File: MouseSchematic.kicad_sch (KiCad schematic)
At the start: 21 parts, among them IC1 AZ1117IH-3.3TRG1, J1 JST1, J2 JST2, J3 Left Header, J4 Right Header, Q1 MOSFET, Q2 IR Receiver, U1 L293DD

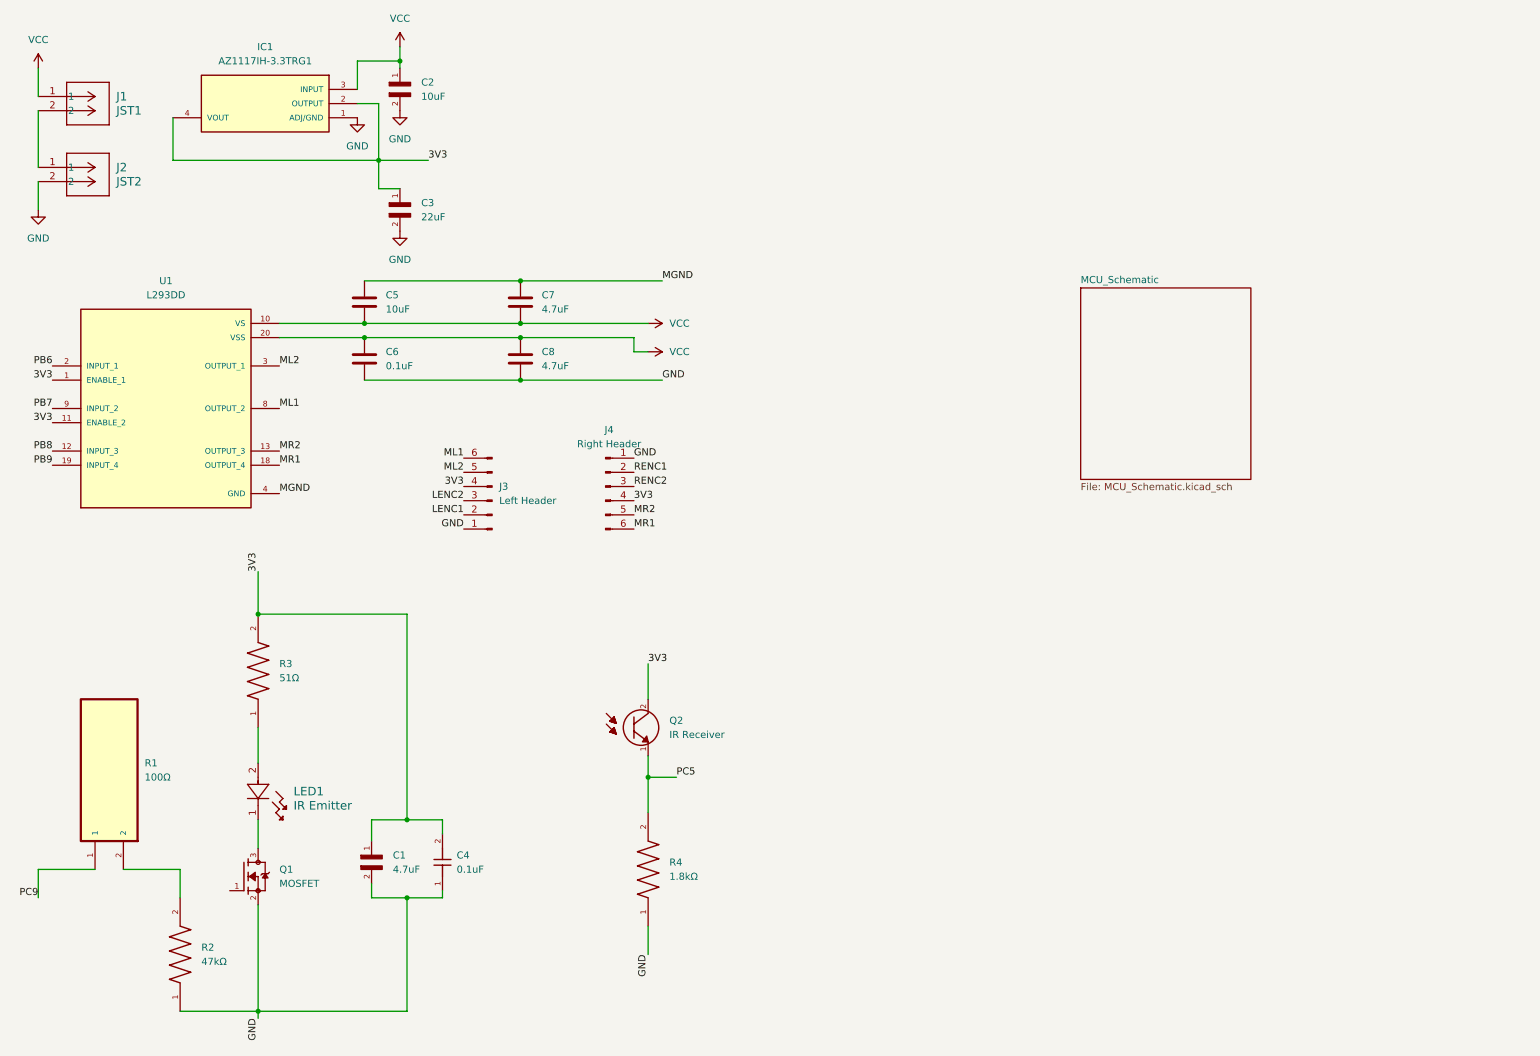
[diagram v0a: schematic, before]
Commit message: Added microcontroller, organized
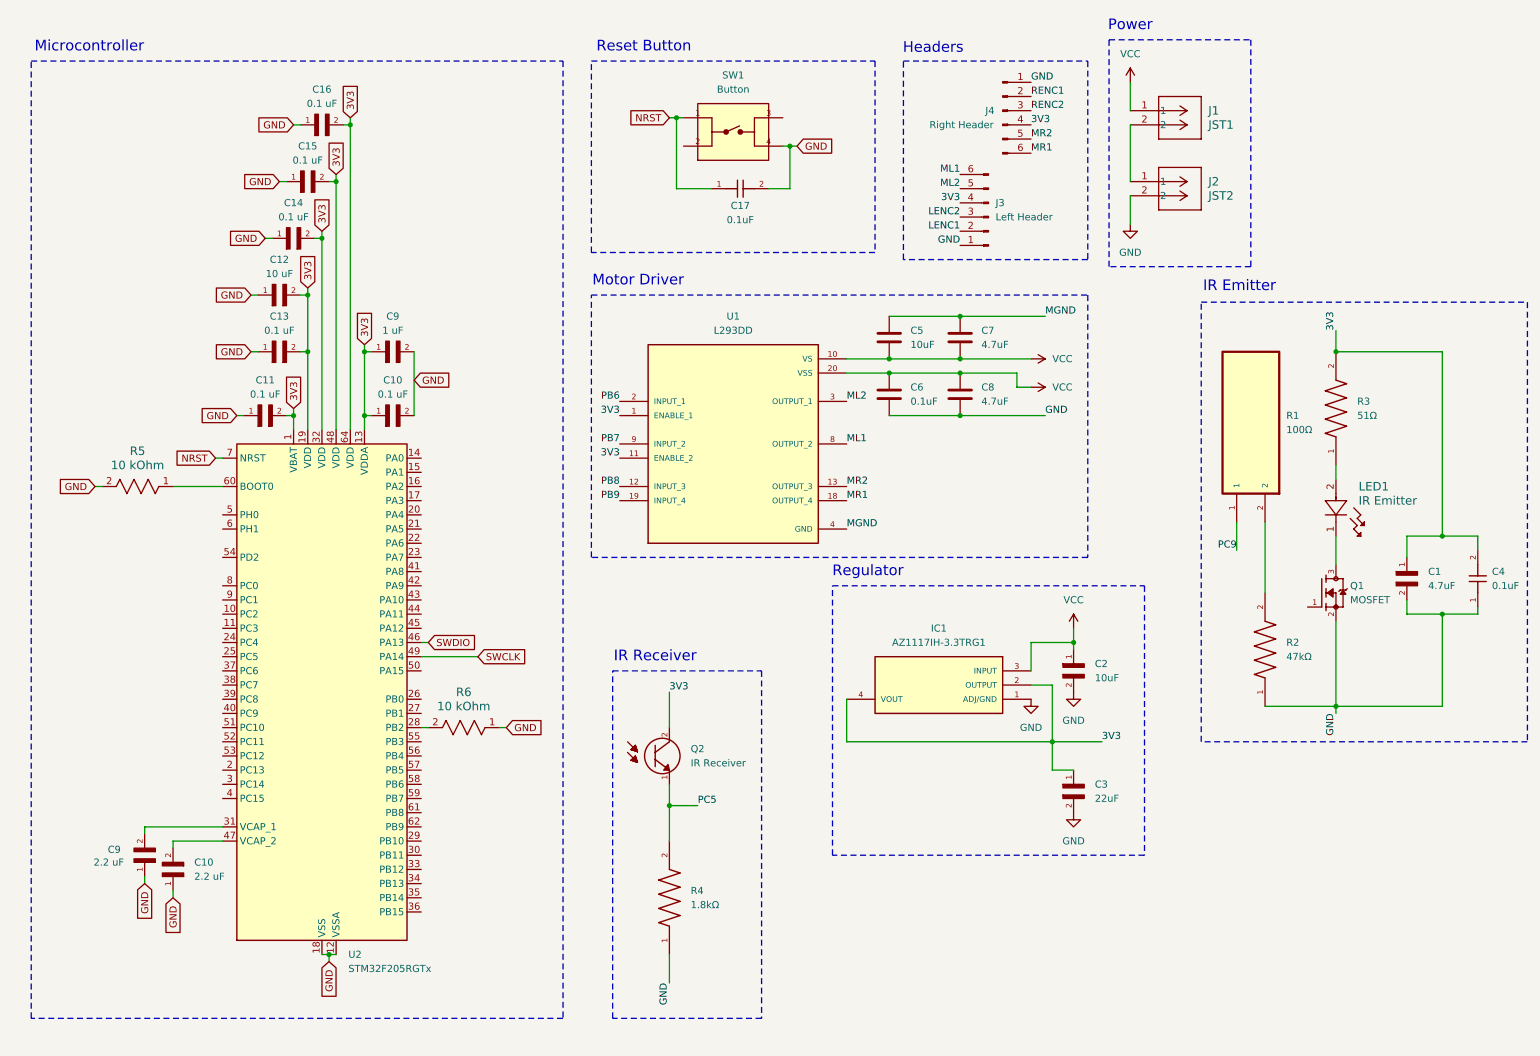
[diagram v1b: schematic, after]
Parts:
- added C10, C9: 2.2 uF, 10uF_Capacitor_FP_GRM188R61C106MAALD:CAPC1608X95N, symbol 10uF_Capacitor_GRM188R61C106MAALD:GRM188R61C106MAALD
- added C10, C11, C13, C14, C15, C16: 0.1 uF, 10uF_Capacitor_FP_GRM188R61C106MAALD:CAPC1608X95N, symbol 10uF_Capacitor_GRM188R61C106MAALD:GRM188R61C106MAALD
- added C12: 10 uF, 10uF_Capacitor_FP_GRM188R61C106MAALD:CAPC1608X95N, symbol 10uF_Capacitor_GRM188R61C106MAALD:GRM188R61C106MAALD
- added C17: 0.1uF, C0805C104K5RACTU:CAPC2012X88N, symbol Capacitor0.1u_C0805C104K5RACTU:C0805C104K5RACTU
- added C9: 1 uF, 10uF_Capacitor_FP_GRM188R61C106MAALD:CAPC1608X95N, symbol 10uF_Capacitor_GRM188R61C106MAALD:GRM188R61C106MAALD
- added R5, R6: 10 kOhm, 51Ohm_Resistor_FP:RES_RK73B_1J_KOA, symbol 51Ohm_Resistor:RK73B1JTTD510J
- added SW1: Button, Button_FP_FSM4JSMA:TE_FSM4JSMA, symbol Button_FSM4JSMA:FSM4JSMA
- added U2: STM32F205RGTx, Package_QFP:LQFP-64_10x10mm_P0.5mm, symbol MCU_ST_STM32F2:STM32F205RGTx
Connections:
- net 3V3: now also C10.1, C11.2, C12.2, C13.2, C14.2, C15.2, C16.2, C9.1, U2.1 (VBAT), U2.13 (VDDA), U2.19 (VDD), U2.32 (VDD), U2.48 (VDD), U2.64 (VDD)
- net GND: now also C10.1, C10.2, C11.1, C12.1, C13.1, C14.1, C15.1, C16.1, C17.2, C9.1, C9.2, R5.2, R6.1, SW1.4, U2.12 (VSSA), U2.18 (VSS), U2.63 (VSS)
- new net: C10.2, U2.47 (VCAP_2)
- new net: R6.2, U2.28 (PB2)
- new net: C9.2, U2.31 (VCAP_1)
- new net: R5.1, U2.60 (BOOT0)
- new net NRST: C17.1, SW1.1, U2.7 (NRST)
- new net SWCLK: U2.49 (PA14)
- new net SWDIO: U2.46 (PA13)
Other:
- removed sheet MCU_Schematic
- note added: "Headers"
- note added: "IR Emitter"
- note added: "IR Receiver"
- note added: "Microcontroller"
- note added: "Motor Driver"
- note added: "Power"
- note added: "Regulator"
- note added: "Reset Button"
- moved on the sheet: C1, C2, C3, C4, C5, C6, C7, C8, IC1, J1, J2, J3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

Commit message: Finished schematic wiring
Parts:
- added C18, C20, C22: 4.7uF, C2012X7R1C475K125AE:CAPC2012X150N, symbol Capacitor4.7u_C2012X7R1C475K125AE:C2012X7R1C475K125AE
- added C19, C21, C23: 0.1uF, C0805C104K5RACTU:CAPC2012X88N, symbol Capacitor0.1u_C0805C104K5RACTU:C0805C104K5RACTU
- added J6: Conn_01x04, symbol Connector_Generic:Conn_01x04
- added LED2, LED3, LED4: IR Emitter, LED_INL-5AMIR15_INO, symbol LED_IR_Emitter_INL-5AMIR15:INL-5AMIR15
- added Q3, Q4, Q5: IR Receiver, SFH_313_FA-3_4:XDCR_SFH_313_FA-3_4, symbol Phototransistor_SFH_313_FA-3_4:SFH_313_FA-3_4
- added Q6, Q7, Q8: MOSFET, 2N7002LT1G:SOT95P240X111-3N, symbol MOSFET_2N7002LT1G:2N7002LT1G
- added R10, R13, R16: 100Ω, ERA-6AEB101V:RESC2012X60N, symbol Resistor100_ERA-6AEB101V:ERA-6AEB101V
- added R11, R14, R17: 47kΩ, ERA6AEB473V:RES_ERA6AEB473V, symbol Resistor47k_ERA_6AEB473V:ERA6AEB473V
- added R12, R15, R18: 51Ω, RC0805FR-0751RL:RESC2012X60N, symbol Resistor51_RC0805FR-0751RL:RC0805FR-0751RL
- added R7, R8, R9: 1.8kΩ, RMCF0805JT1K80:RESC2012X65N, symbol Resistor1.8k_RMCF0805JT1K80:RMCF0805JT1K80
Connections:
- net PB6 is gone; now on an unnamed net: U1.2 (INPUT_1)
- net PB7 is gone; now on an unnamed net: U1.9 (INPUT_2)
- net PB8 is gone; now on an unnamed net: U1.12 (INPUT_3)
- net PB9 is gone; now on an unnamed net: U1.19 (INPUT_4)
- net PC9 is gone; now on an unnamed net: R1.1
- net 3V3: now also C18.1, C19.2, C20.1, C21.2, C22.1, C23.2, Q3.2, Q4.2, Q5.2, R12.2, R15.2, R18.2
- net GND: now also C18.2, C19.1, C20.2, C21.1, C22.2, C23.1, J6.3 (Pin_3), Q6.2, Q7.2, Q8.2, R11.1, R14.1, R17.1, R7.1, R8.1, R9.1
- net LENC1: now also U2.42 (PA9)
- net LENC2: now also U2.41 (PA8)
- net PC5: now also U2.25 (PC5)
- net RENC1: now also U2.15 (PA1)
- net RENC2: now also U2.14 (PA0)
- net SWCLK: now also J6.4 (Pin_4)
- net SWDIO: now also J6.2 (Pin_2)
- net NSRT: now reaches SW1.3
- net NSRT: now also J6.1 (Pin_1)
- net PA6: now reaches U2.22 (PA6)
- net PA6: now also Q4.1, R8.2
- net PA7: now reaches U2.23 (PA7)
- net PA7: now also R13.1
- net PC4: now reaches U2.24 (PC4)
- net PC4: now also Q3.1, R7.2
- net PB1: now reaches U2.27 (PB1)
- net PB1: now also Q5.1, R9.2
- net PB13: now reaches U2.34 (PB13)
- net PB13: now also R10.1
- net PB3: now reaches U2.55 (PB3)
- net PB3: now also R16.1
- new net: LED2.1, Q6.3
- new net: LED2.2, R12.1
- new net: R16.2, R17.2
- new net: LED3.1, Q7.3
- new net: LED3.2, R15.1
- new net: R13.2, R14.2
- new net: R10.2, R11.2
- new net: LED4.1, Q8.3
- new net: LED4.2, R18.1
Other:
- note added: "Front Left IR Emitter"
- note added: "Front Left IR Receiver"
- note added: "Left IR Emitter"
- note added: "Left IR Receiver"
- note added: "Right IR Emitter"
- note added: "Right IR Receiver"
- moved on the sheet: C1, C17, C2, C3, C4, C5, C6, C7, C8, IC1, J3, J4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

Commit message: Schematic review
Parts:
- removed C10, C11, C13, C14, C15, C16: 0.1 uF, 10uF_Capacitor_FP_GRM188R61C106MAALD:CAPC1608X95N, symbol 10uF_Capacitor_GRM188R61C106MAALD:GRM188R61C106MAALD
- added C10, C12, C4, C5, C6, C7: 0.1uF, C0805C104K5RACTU:CAPC2012X88N, symbol Capacitor0.1u_C0805C104K5RACTU:C0805C104K5RACTU
- J4: renamed from J1; footprint CONN2_B2B-PH-K-S_JST -> B2B-PH-K-S:CONN2_B2B-PH-K-S_JST
- J5: renamed from J2; footprint CONN2_B2B-PH-K-S_JST -> B2B-PH-K-S:CONN2_B2B-PH-K-S_JST
- LED1, LED2, LED3, LED4: footprint LED_INL-5AMIR15_INO -> INL-5AMIR15:LED_INL-5AMIR15_INO
- renumbered C17 to C1, C4 to C11, C9 to C13, C8 to C14, C7 to C15, C6 to C16, C5 to C17, C19 to C18, C18 to C19, C9 to C2, C2 to C24, C3 to C25, C10 to C3, C12 to C8, C1 to C9, J6 to J1, J3 to J2, J4 to J3, Q6 to Q4, Q4 to Q5, Q7 to Q6, Q8 to Q7, Q5 to Q8, R13 to R11, R14 to R12, R8 to R13, R15 to R14, R16 to R15, R17 to R16, R18 to R17, R9 to R18, R5 to R3, R3 to R4, R6 to R5, R4 to R6, R12 to R8, R11 to R9, U2 to U1, U1 to U2
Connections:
- net 3V3: now also C10.2, C12.1, C4.2, C5.2, C6.2, C7.2
- net GND: now also C10.1, C12.2, C4.1, C5.1, C6.1, C7.1
- net at R15.2, R16.2: now also Q7.1
- net at R1.2, R2.2: now also Q1.1
- net at R11.2, R12.2: now also Q6.1
- net at R10.2, R9.2: now also Q4.1
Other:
- moved on the sheet: C1, C11, C13, C14, C15, C16, C17, C18, C19, C2, C20, C21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

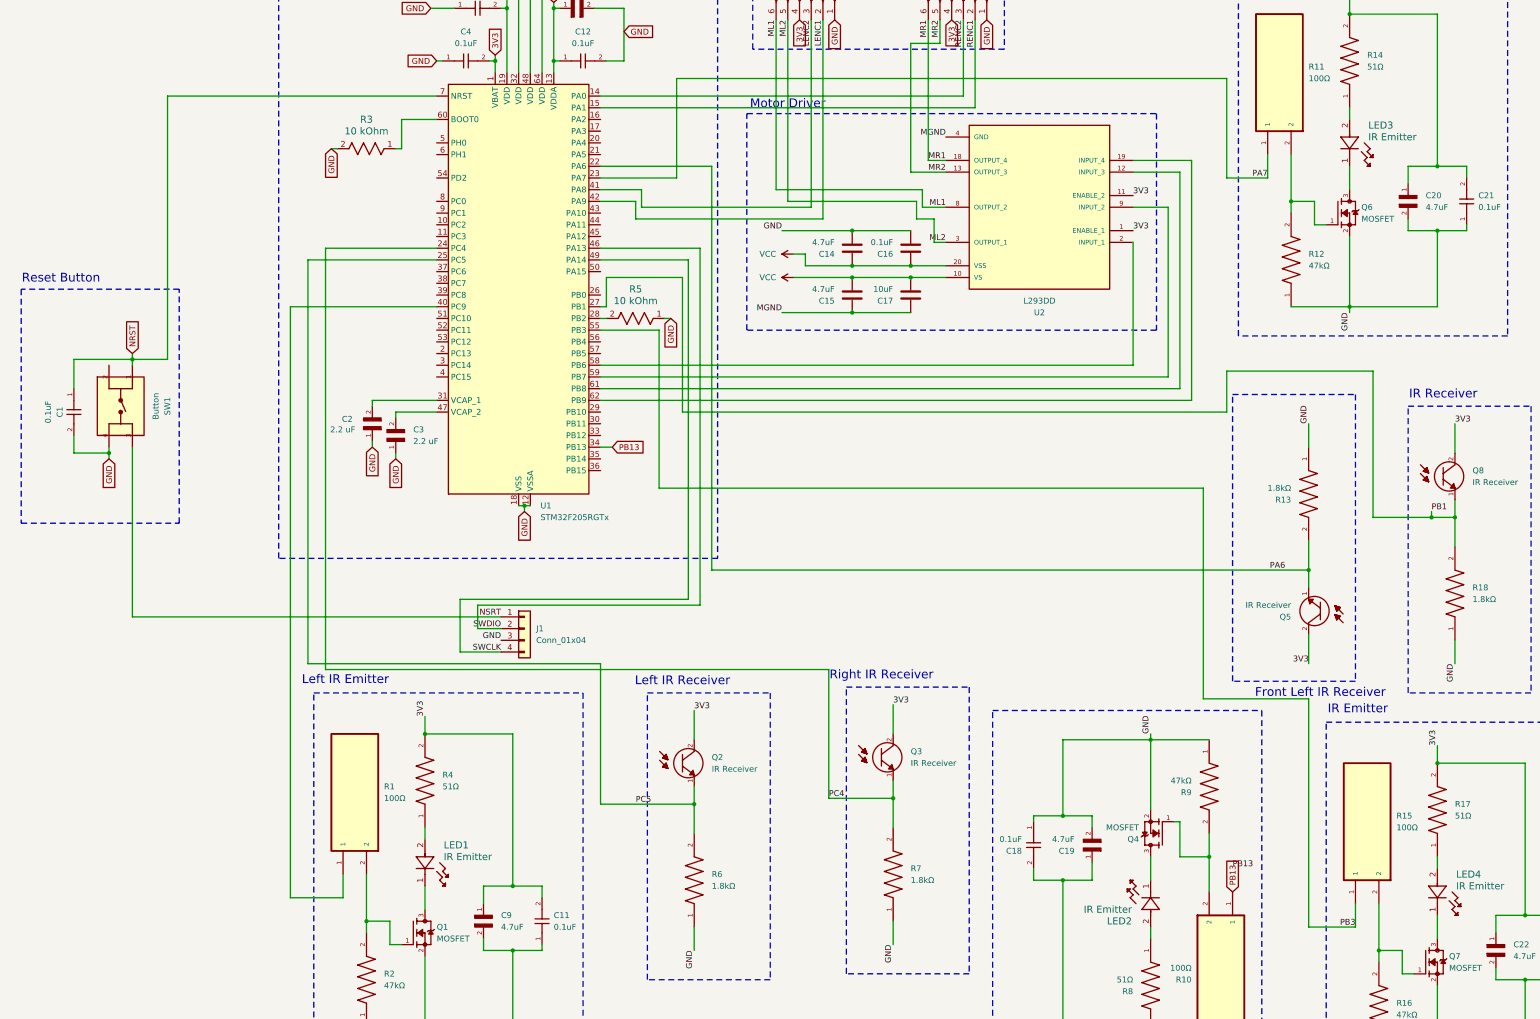
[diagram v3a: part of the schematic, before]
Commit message: Update schematic with more global labels (still need to finish reviewing)
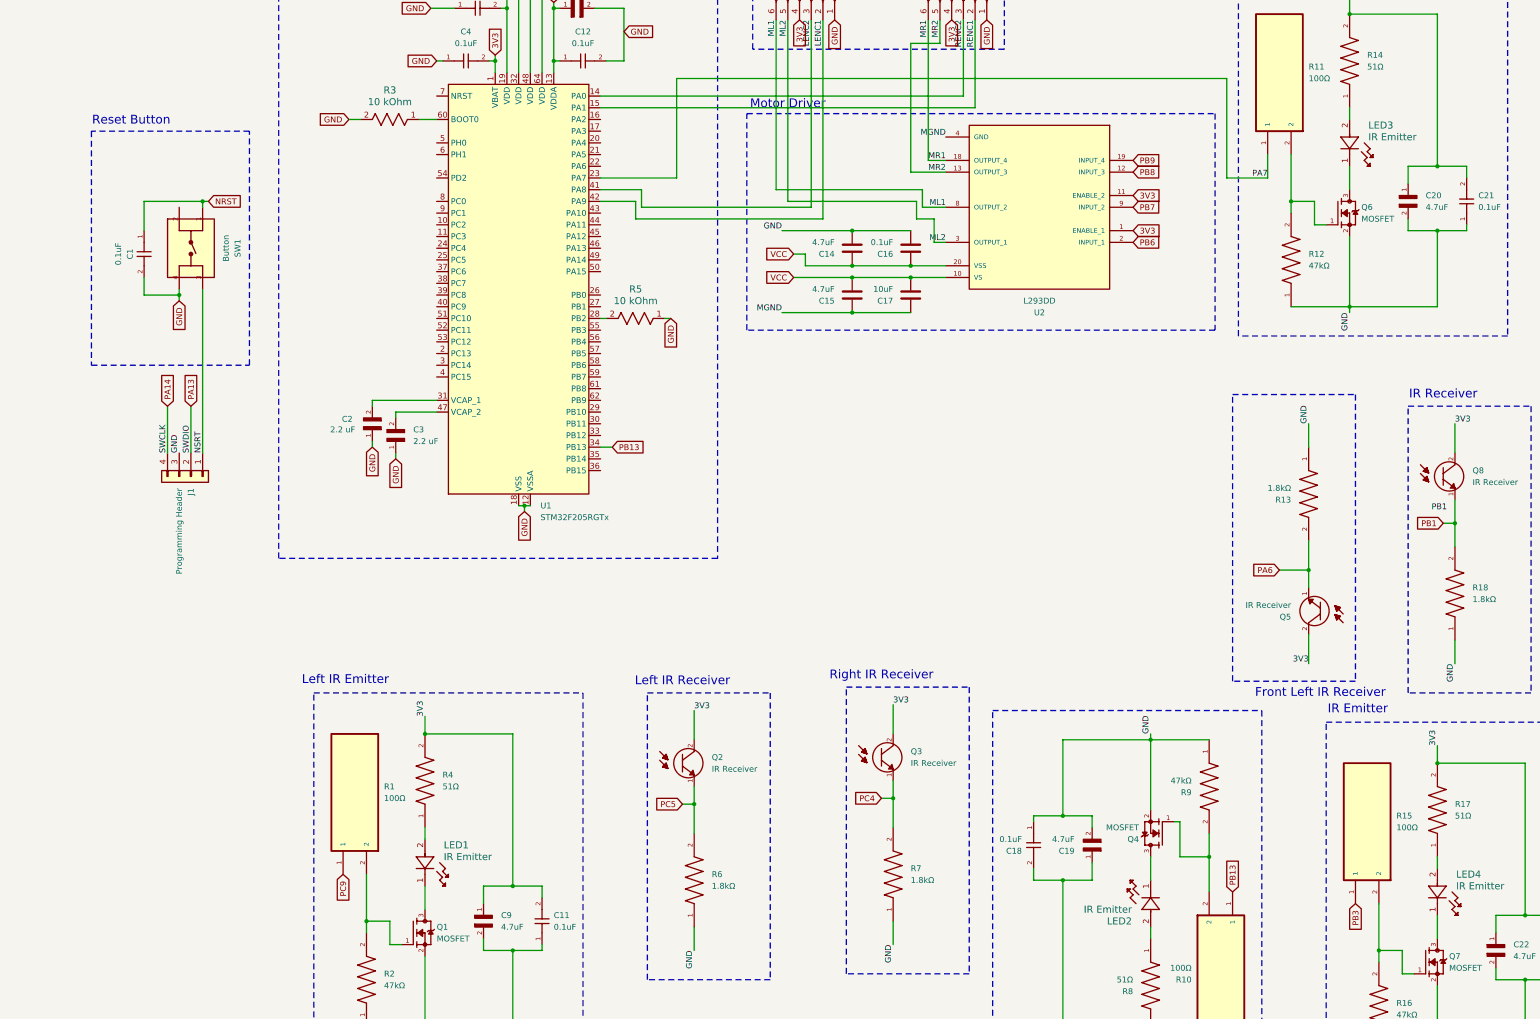
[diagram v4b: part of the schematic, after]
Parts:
- J1: value Conn_01x04 -> Programming Header
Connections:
- net NRST: no longer U1.7 (NRST)
- net PA6: no longer U1.22 (PA6)
- net PB1: no longer U1.27 (PB1)
- net PB3: no longer U1.55 (PB3)
- net PC4: no longer U1.24 (PC4)
- net PC5: no longer U1.25 (PC5)
- net at U1.40 (PC9): no longer R1.1
- net at U1.58 (PB6): no longer U2.2 (INPUT_1)
- net at U1.59 (PB7): no longer U2.9 (INPUT_2)
- net at U1.61 (PB8): no longer U2.12 (INPUT_3)
- net at U1.62 (PB9): no longer U2.19 (INPUT_4)
- net SWCLK: no longer names the net of U1.49 (PA14)
- net SWCLK: no longer J1.4 (Pin_4)
- net SWDIO: no longer names the net of U1.46 (PA13)
- net SWDIO: no longer J1.2 (Pin_2)
- new net PA13: J1.2 (Pin_2)
- new net PA14: J1.4 (Pin_4)
- new net PB6: U2.2 (INPUT_1)
- new net PB7: U2.9 (INPUT_2)
- new net PB8: U2.12 (INPUT_3)
- new net PB9: U2.19 (INPUT_4)
- new net PC9: R1.1
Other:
- moved on the sheet: C1, J1, R3, SW1

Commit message: Added power LED, updated certain resistors and capacitors to match requirements
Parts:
- removed C13: 1 uF, 10uF_Capacitor_FP_GRM188R61C106MAALD:CAPC1608X95N, symbol 10uF_Capacitor_GRM188R61C106MAALD:GRM188R61C106MAALD
- removed C14, C15: 4.7uF, symbol Device:C
- removed C16: 0.1uF, symbol Device:C
- removed C17: 10uF, symbol Device:C
- removed C2, C3: 2.2 uF, 10uF_Capacitor_FP_GRM188R61C106MAALD:CAPC1608X95N, symbol 10uF_Capacitor_GRM188R61C106MAALD:GRM188R61C106MAALD
- removed R1, R10, R11, R15: 100Ω, ERA-6AEB101V:RESC2012X60N, symbol Resistor100_ERA-6AEB101V:ERA-6AEB101V
- added C11, C19: 2.2uF, CL21B225KAFNNNE:CAPC2012X135N, symbol Capacitor2.2u_CL21B225KAFNNNE:CL21B225KAFNNNE
- added C20, C22: 4.7uF, C2012X7R1C475K125AE:CAPC2012X150N, symbol Capacitor4.7u_C2012X7R1C475K125AE:C2012X7R1C475K125AE
- added C21: 10uF, CL21B106KOQNNNE:CAPC2012X140N, symbol Capacitor_CL21B106KOQNNNE:CL21B106KOQNNNE
- added C23: 1uF, CL21B105KBFNNNE:CAPC2012X135N, symbol Capacitor1u_CL21B105KBFNNNE:CL21B105KBFNNNE
- added C26: 0.1uF, C0805C104K5RACTU:CAPC2012X88N, symbol Capacitor0.1u_C0805C104K5RACTU:C0805C104K5RACTU
- added D1: LED, symbol Device:LED
- added R16, R5, R7, R9: 100Ω, CRCW0805100RFKEA:RESC2012X50N, symbol Resistor100_CRCW0805100RFKEA:CRCW0805100RFKEA
- added R19: R_US, symbol Device:R_US
- renumbered C18 to C1, C4 to C12, C5 to C13, C6 to C14, C7 to C15, C8 to C16, C10 to C17, C12 to C18, C19 to C2, C22 to C3, C20 to C4, C9 to C5, C23 to C6, C21 to C7, C11 to C8, C1 to C9, J3 to J2, J2 to J3, LED4 to LED1, LED3 to LED2, LED1 to LED3, LED2 to LED4, Q2 to Q1, Q8 to Q2, Q5 to Q4, Q7 to Q5, Q1 to Q7, Q4 to Q8, R6 to R1, R2 to R10, R17 to R11, R14 to R12, R4 to R13, R8 to R14, R9 to R15, R3 to R17, R5 to R18, R18 to R2, R7 to R3, R13 to R4, R16 to R6, R12 to R8
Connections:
- net 3V3: now also C23.1, D1.2 (A)
- net GND: now also C11.1, C19.1, C20.1, C21.1, C22.2, C23.2, C26.1, R19.2
- net PA7: now also R7.2; no longer U1.23 (PA7)
- net PB13: now also R16.1
- net PB3: now also R5.2
- net PC9: now also R9.2
- net VCC: now also C20.2, C21.2, C22.1, C26.2
- net at U1.47 (VCAP_2): now also C11.2
- net at U1.31 (VCAP_1): now also C19.2
- net at Q5.1, R6.2: now also R5.1
- net at Q7.1, R10.2: now also R9.1
- net at Q6.1, R8.2: now also R7.1
- net at Q8.1, R15.2: now also R16.2
- net LENC1: no longer names the net of U1.42 (PA9)
- net LENC1: no longer J3.2 (Pin_2)
- net LENC2: no longer names the net of U1.41 (PA8)
- net LENC2: no longer J3.3 (Pin_3)
- net RENC1: no longer names the net of U1.15 (PA1)
- net RENC1: no longer J2.2 (Pin_2)
- net RENC2: no longer names the net of U1.14 (PA0)
- net RENC2: no longer J2.3 (Pin_3)
- new net: D1.1 (K), R19.1
- new net PA0: J2.3 (Pin_3)
- new net PA1: J2.2 (Pin_2)
- new net PA8: J3.3 (Pin_3)
- new net PA9: J3.2 (Pin_2)
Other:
- note added: "Front Right IR Emitter"
- note added: "Front Right IR Receiver"
- note added: "Power LED"
- note added: "Power Switch"
- note removed: "IR Emitter"
- note removed: "IR Receiver"
- moved on the sheet: C1, C12, C13, C14, C15, C16, C17, C18, C2, C24, C25, C3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
